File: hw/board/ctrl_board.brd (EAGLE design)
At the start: 101.6 x 101.3 mm, 64 parts, among them IC1 7805T

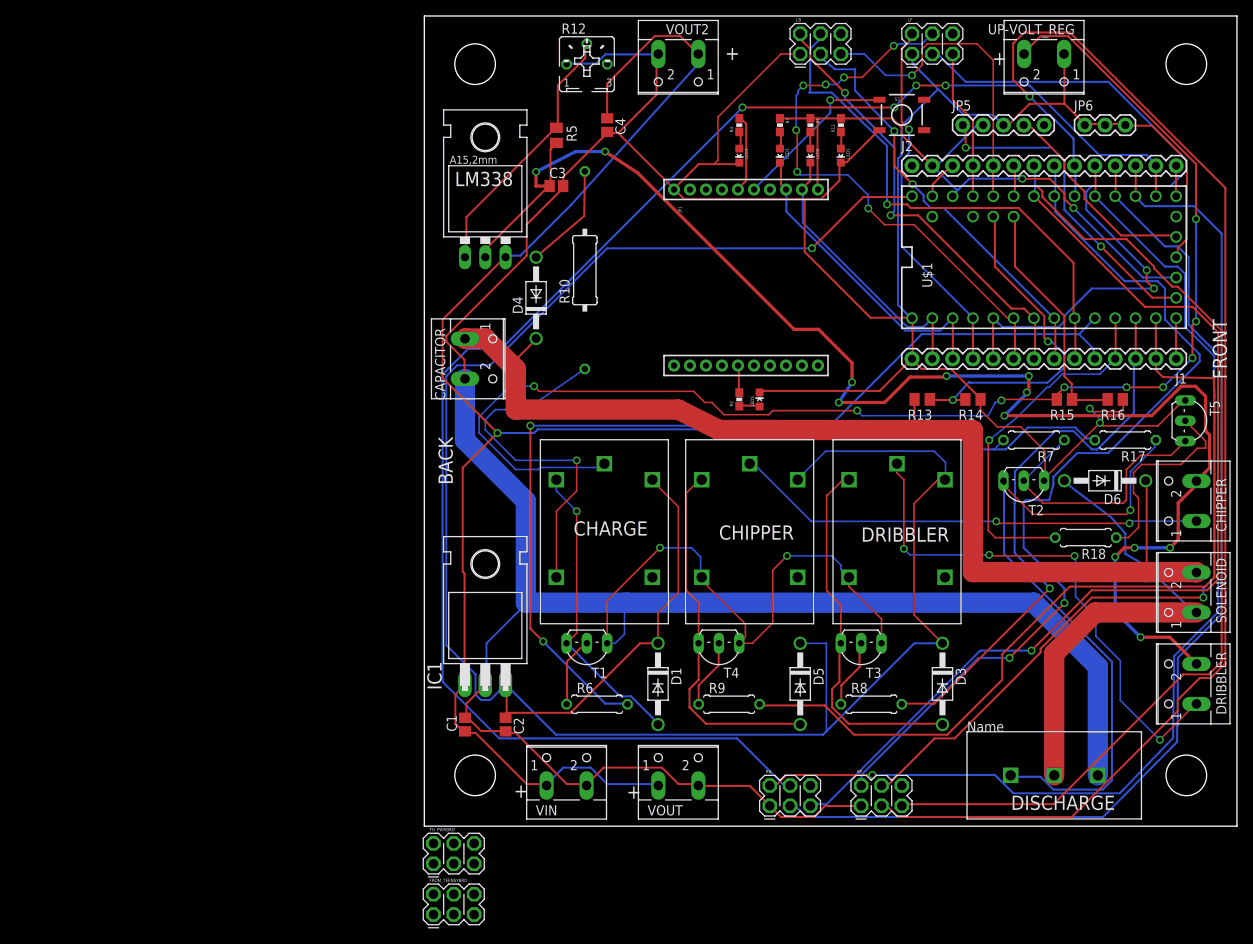
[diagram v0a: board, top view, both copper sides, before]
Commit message: separation in two boards - work in progress
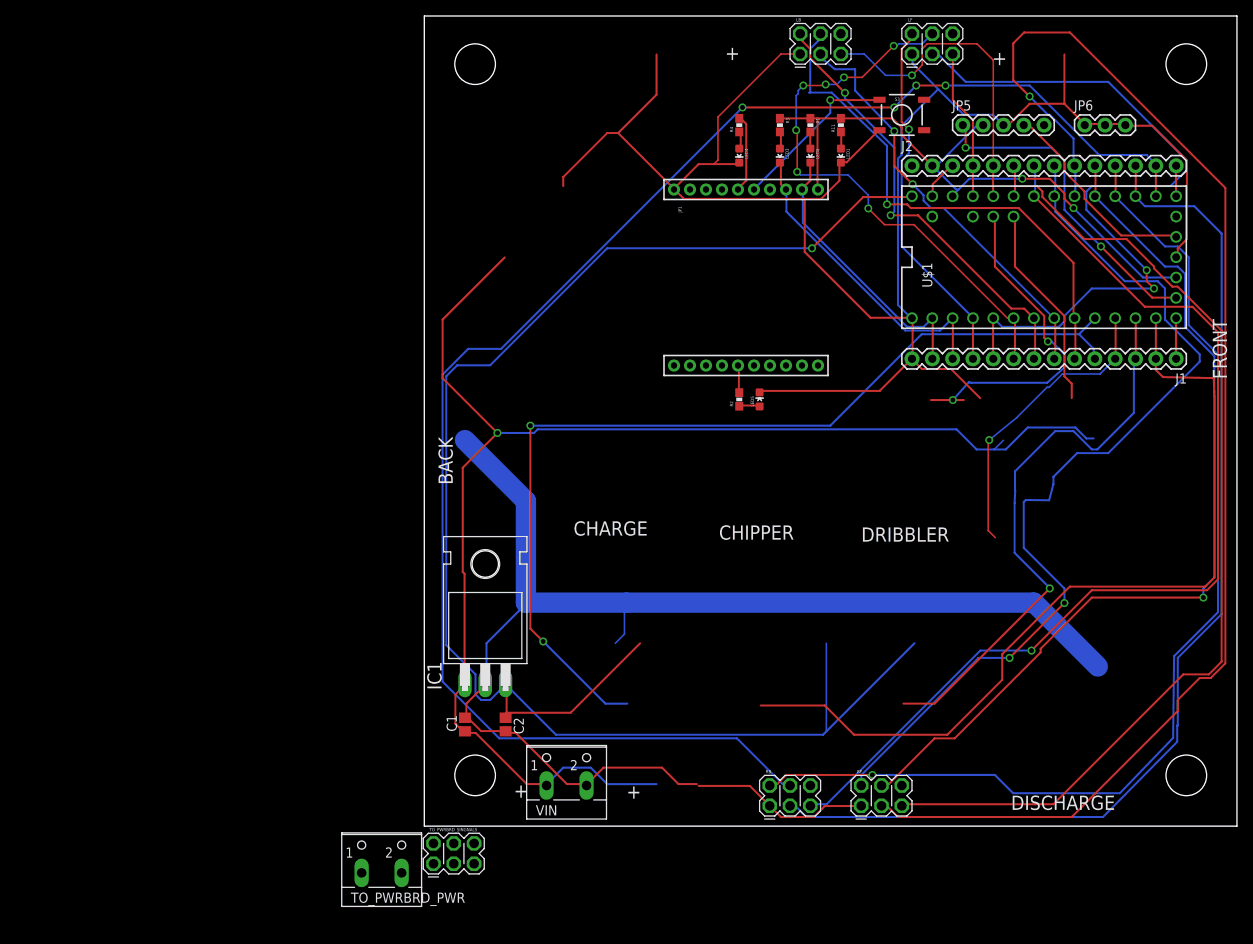
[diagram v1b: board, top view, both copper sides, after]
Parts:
- removed C3: 1uF, adafruit:C0805
- removed C4: 0.1uF, adafruit:C0805
- removed CAPACITOR, CHIPPER, DRIBBLER, SOLENOID, VOUT, VOUT2: (no value), con-wago-500:W237-102
- removed D1, D3, D4, D5, D6: 1N4004, diode:DO41-10
- removed FROM_TEENSYBRD: (no value), SparkFun-Connectors:2X3_POGO
- removed LM338: (no value), v-reg:317TL
- removed R10: 2k_1W, resistor:0309/12
- removed R12: 5k, pot:B25P
- removed R13, R15: 1M, resistor:M0805
- removed R14, R16: 10k, resistor:M0805
- removed R17, R7: 10k, resistor:0207/7
- removed R18: 1k, resistor:0207/7
- removed R5: 120, resistor:M0805
- removed R6, R8, R9: (no value), resistor:0207/7
- removed T1, T2, T3, T4, T5: (no value), transistor-neu-to92:TO92-EBC
- removed U$2: APT75GN120LG, igbt:TO-264
- removed U$3, U$4, U$5: PANASONIC_JS1, RoboBulls_relay:PANASONIC_JS1
- removed UP-VOLT_REG: +, con-wago-500:W237-102
- added TO_PWRBRD_PWR: (no value), con-wago-500:W237-102
- renumbered TO_PWRBRD to TO_PWRBRD_SINGNALS
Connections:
- removed net +12V: C3.1, CHIPPER.2, DRIBBLER.2, LM338.2, R5.2
- removed net N$10: R10.1, U$3.P$4
- removed net N$11: D6.A, SOLENOID.1, U$2.COLLECTORPAD
- removed net N$13: CAPACITOR.1, D4.C, D6.C, R13.2, SOLENOID.2
- removed net N$14: R15.2, U$3.P$1, UP-VOLT_REG.2
- removed net N$15: R6.1, T1.B
- removed net N$2: LM338.1, R12.S, R5.1
- removed net N$20: R8.1, T3.B
- removed net N$22: DRIBBLER.1, U$4.P$1
- removed net N$24: D5.A, T4.C, U$5.P$5
- removed net N$26: R9.1, T4.B
- removed net N$28: CHIPPER.1, U$5.P$1
- removed net N$3: R18.1, T5.B
- removed net N$4: R7.1, T2.B, T5.C
- removed net N$5: R17.1, T2.C, U$2.GATEPAD
- removed net N$6: D1.A, T1.C, U$3.P$5
- removed net N$8: D3.A, T3.C, U$4.P$5
- removed net N$9: D4.A, R10.2
- removed net PWR_CHARGE: FROM_TEENSYBRD.P$5
- removed net PWR_CHIP: FROM_TEENSYBRD.P$6
- removed net PWR_DISCHARGE: FROM_TEENSYBRD.P$2
- removed net PWR_DRIBBLE: FROM_TEENSYBRD.P$4
- removed net PWR_READ_250: FROM_TEENSYBRD.P$1
- removed net PWR_READ_CAP: FROM_TEENSYBRD.P$3
- net +24V: now also TO_PWRBRD_PWR.1; no longer C4.1, LM338.3, R17.2, R7.2, VOUT.1, VOUT2.1
- net +5V: no longer D1.C, D3.C, D5.C, U$3.P$2, U$4.P$2, U$5.P$2
- net CHARGE: no longer R6.2
- net CHIP: no longer R9.2
- net DISCHARGE: no longer R18.2
- net DRIBBLE: no longer R8.2
- net GND: now also TO_PWRBRD_PWR.2; no longer C3.2, C4.2, CAPACITOR.2, R12.A, R14.1, R16.1, T1.E, T2.E, T3.E, T4.E, T5.E, U$2.EMITTERPAD, U$4.P$4, U$5.P$4, UP-VOLT_REG.1, VOUT.2, VOUT2.2
- net READ_250: no longer R15.1, R16.2
- net READ_CAP: no longer R13.1, R14.2
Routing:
- net +12V: track 184.7 -> 0.00 mm, vias 12 -> 0
- net GND: track 603.3 -> 423.9 mm, vias 4 -> 0
- net N$14: track 169.8 -> 0.00 mm, vias 9 -> 0
- net N$13: track 136.3 -> 0.00 mm
- net N$5: track 84.9 -> 0.00 mm, vias 2 -> 0
- net +5V: track 287.1 -> 208.5 mm
- net N$22: track 66.5 -> 0.00 mm, vias 4 -> 0
- net N$11: track 59.8 -> 0.00 mm
- net N$28: track 59.7 -> 0.00 mm, vias 2 -> 0
- net +24V: track 231.8 -> 175.8 mm
- net N$8: track 46.2 -> 0.00 mm
- net N$24: track 45.2 -> 0.00 mm
- net N$10: track 44.5 -> 0.00 mm, vias 1 -> 0
- net N$6: track 37.8 -> 0.00 mm, vias 1 -> 0
- net N$4: track 34.2 -> 0.00 mm
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
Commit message: Added power connectors to ctrl board, fix pwr board error
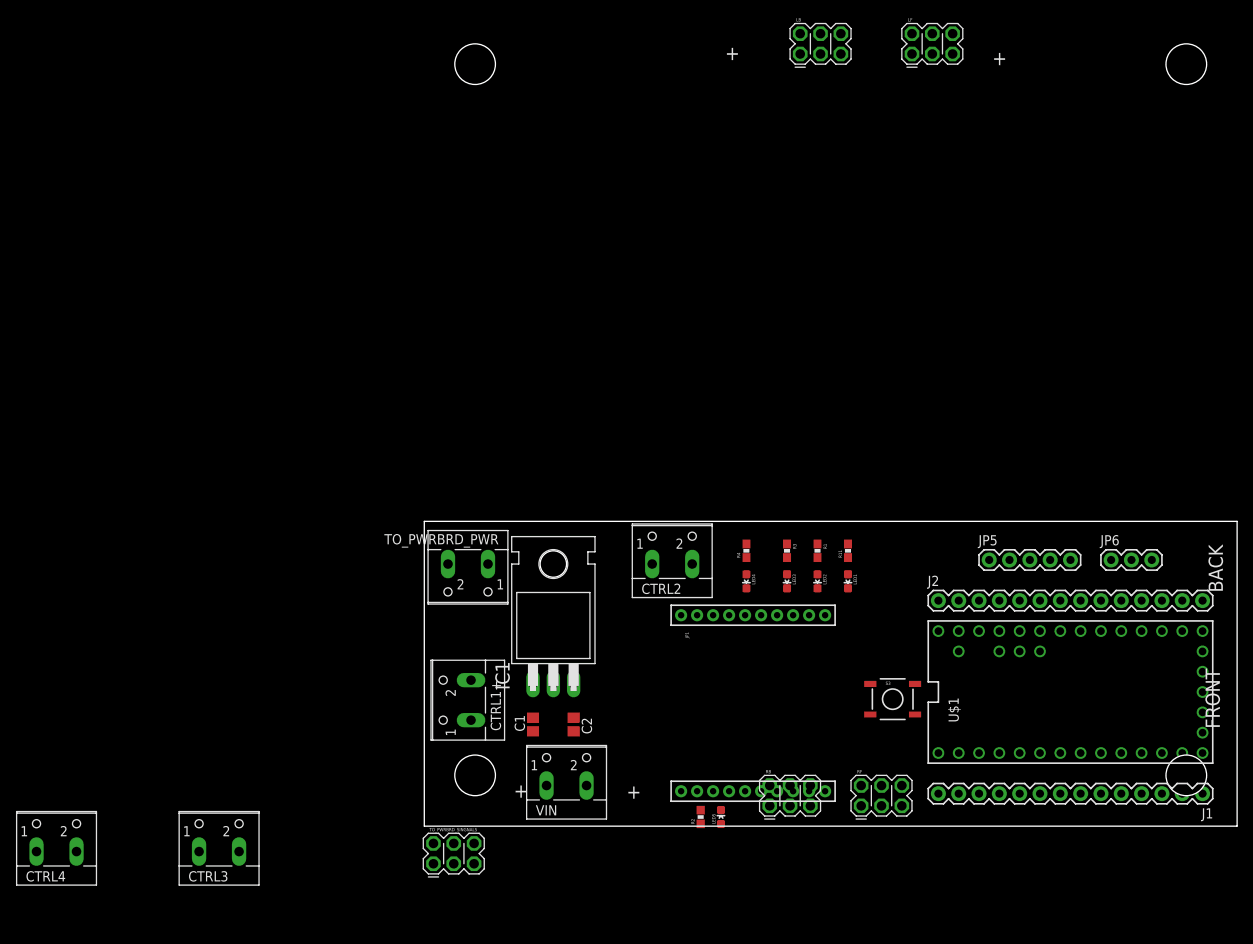
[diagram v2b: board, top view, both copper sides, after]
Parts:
- added CTRL1+, CTRL2, CTRL3, CTRL4: (no value), con-wago-500:W237-102
- moved S3 73.0 mm to (58.5, 15.9)
- moved U$1 54.5 mm to (80.8, 16.8)
- moved J1 54.5 mm to (97.3, 4.06)
- moved J2 54.5 mm to (64.3, 28.2)
- moved JP5 54.5 mm to (70.6, 33.3)
- moved JP6 54.5 mm to (85.9, 33.3)
- moved JP1 53.2 mm to (30.1, 15.4)
- moved LED1 53.2 mm to (53.0, 30.6)
- moved LED2 53.2 mm to (49.1, 30.6)
- moved LED3 53.2 mm to (45.3, 30.6)
- moved LED4 53.2 mm to (40.3, 30.6)
- moved R1 53.2 mm to (49.1, 34.4)
- moved R11 53.2 mm to (53.0, 34.4)
- moved R3 53.2 mm to (45.3, 34.4)
- moved R4 53.2 mm to (40.3, 34.4)
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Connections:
- new net N$2: CTRL1+.1, CTRL2.1
- net +24V: now also CTRL3.1, CTRL4.1
- net GND: now also CTRL1+.2, CTRL2.2, CTRL3.2
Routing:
- net GND: track 423.9 -> 0.00 mm
- net +5V: track 208.5 -> 0.00 mm, vias 1 -> 0
- net RBBRK: track 199.5 -> 0.00 mm, vias 4 -> 0
- net +24V: track 175.8 -> 0.00 mm, vias 1 -> 0
- net RFDIR: track 169.4 -> 0.00 mm, vias 1 -> 0
- net RBDIR: track 135.4 -> 0.00 mm
- net RBENA: track 135.0 -> 0.00 mm, vias 1 -> 0
- net RBSPEED: track 127.6 -> 0.00 mm, vias 1 -> 0
- net RFSPEED: track 126.7 -> 0.00 mm
- net CHARGE: track 121.4 -> 0.00 mm, vias 2 -> 0
- net RFENA: track 115.4 -> 0.00 mm, vias 2 -> 0
- net RFBRK: track 112.1 -> 0.00 mm, vias 1 -> 0
- net CHIP: track 107.2 -> 0.00 mm
- net LFDIR: track 95.8 -> 0.00 mm, vias 2 -> 0
- net 3.3V: track 78.5 -> 0.00 mm, vias 2 -> 0
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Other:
- board size 101.6 x 101.3 mm -> 101.6 x 38.1 mm
- board text removed: "CHARGE"
- board text removed: "CHIPPER"
- board text removed: "DISCHARGE"
- board text removed: "DRIBBLER"
